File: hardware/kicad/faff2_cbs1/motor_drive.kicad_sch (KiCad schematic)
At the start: 89 parts, among them J1101 1x6 2.54mm, J1102 1x6 2.54mm, J1103 Micro-Fit 1x3, Q1101 BSZ099N06LS5, Q1102 BSZ099N06LS5, Q1103 BSZ099N06LS5, Q1104 BSZ099N06LS5, Q1105 BSZ099N06LS5, Q1106 BSZ099N06LS5, U1101 DRV8323S

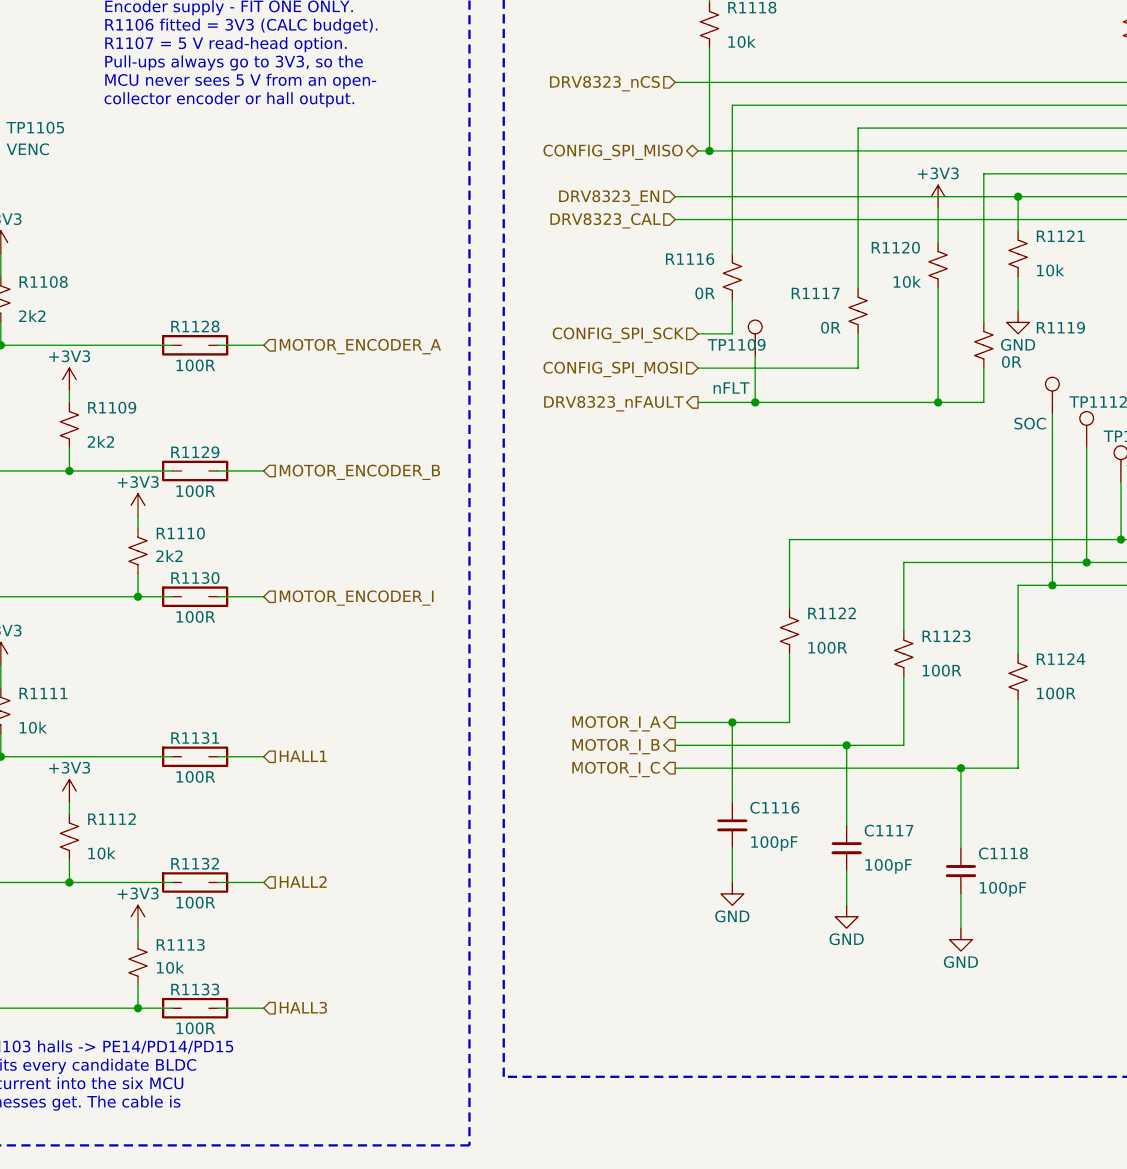
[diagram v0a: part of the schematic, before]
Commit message: review r4 items 7,8,13 and the PWR1131 ruling: parts, not placement
Items 7 and 8, R608 and R609 go. Review round R6 asked for DNP parallel
positions across R601, FB601 and D601; the captain has reversed two of the
three, and the reasoning is better than the original: R608 and R601 are the same
0603, so to meter head current you replace R601 with a shunt rather than
populate a second footprint beside it, and FB601 can be lifted and bridged
instead of fitting R609. D602 stays - a second clamp POSITION, for a different
clamp voltage or a bidirectional part, is not the same argument. Both the sheet
note and actuator-rev-afe.md's R6 row now carry the reversal rather than
quietly dropping it.

Item 13, R1128..R1133 were the only 100R in the design on a project-local
symbol: faff2_passives:RES_TF_100R_0603_H, a pre-rotated variant round 2 added
so they could lie horizontally without instance rotation - that was the reason,
and it does not outweigh nine other 100R across mcu, ui_io and motor_drive using
the house Amodo_Resistors:RES_TF_100R_0603. They unify onto it, rotated 90 with
field angles compensated to 270, which AGENTS.md permits on exactly that
condition and which a render confirms: horizontal body, horizontal text. The
local variant now has no users and is deleted from both the sheet and
faff2_passives, and AGENTS.md's guidance flips to prefer the house symbol.

The captain's third round-3 answer: R1120 and its +3V3 flag drag 7.62 mm down
into the clear space below, same connectivity, and the gate-drive bus no longer
crosses the arrow. No bus reroute, as instructed. Dropping it put R1120's
reference 0.02 mm off R1117's body, so the reference centres in the 6.85 mm
between the two.

The design is now clean under tools/check_text_clearance.py --margin 0.35 for
the first time - zero findings on all ten sheets.

ERC 0/0 at severity-all; 406 components, 264 nets. The only netlist change is
the two removals.

Co-Authored-By: Claude Opus 5 <noreply@anthropic.com>
Claude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
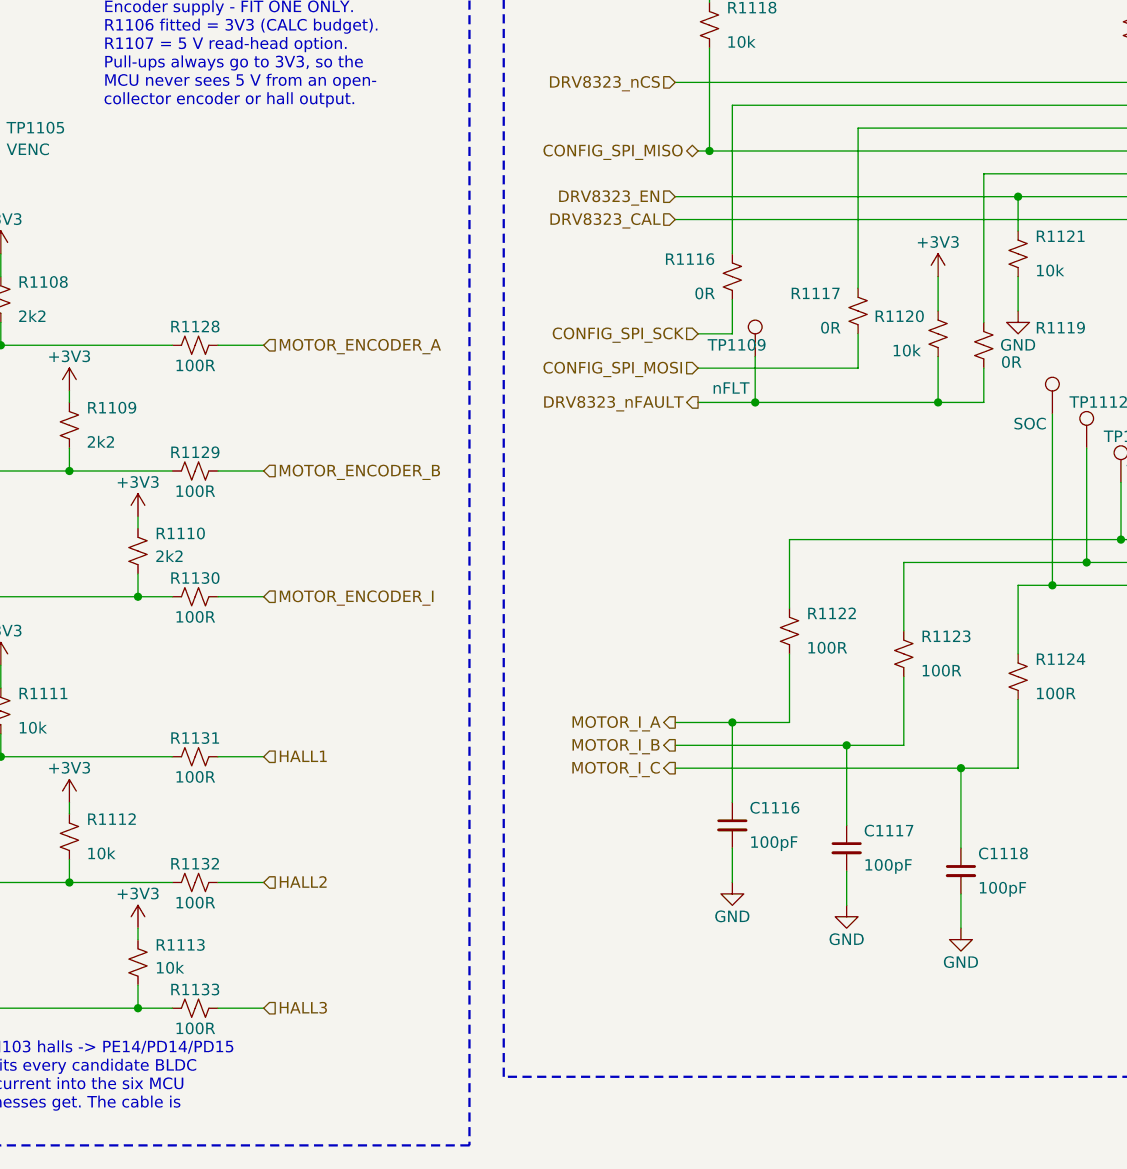
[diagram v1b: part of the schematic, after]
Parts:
- R1128, R1129, R1130, R1131, R1132, R1133: symbol faff2_passives:RES_TF_100R_0603_H -> Amodo_Resistors:RES_TF_100R_0603
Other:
- moved on the sheet: R1120

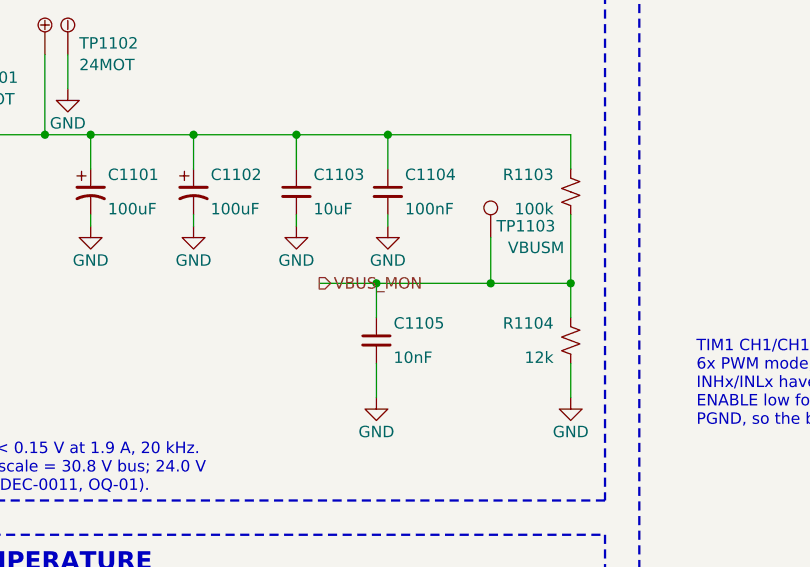
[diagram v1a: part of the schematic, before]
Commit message: review r4: the captain's two power answers - PG into RAIL_PGOOD, +5V5 to 6 V
A1. Both ADPL42005 power-good pins join DEC-P9's wired-AND. R317 and R318, 1 k
each like R315/R316, from each PG down to a local RAIL_PGOOD label - the idiom
the sheet already uses to reach that node three times. A dead 5 V rail is now
visible at D303 and TP308, which is the gap round 3 raised.

A2. +5V5 becomes 6.110 V nominal. The captain asked for 6.0 V - the
ADPL42005's characterised VIN = VOUT + 1 V point - or slightly above only if the
tolerance stack needs it to guarantee a 6.0 V minimum. It does: the LMR33630's
feedback reference is 0.985/1.000/1.015 V, +/-1.5% over the operating range, so
a 100k/20k divider gives 5.900/6.000/6.100 - nominal exactly on target, floor
100 mV short. 64.9k/12.7k gives 6.009/6.110/6.212 and the floor clears. Both
options and the arithmetic are in DEC-P10, along with what else moves: divider
impedance 122.1k to 77.6k so the 50 nA FB bias costs 3.2 mV, duty 0.255 at 24 V
in, caps still better than 2.5x derated, LDO dissipation 139 mW worst case.

Two traps on the way, both worth the tools that caught them. Hand-building the
new resistor block assembled its effects string with a str.replace on
"\t\t\t)", which also matched the font block's closing paren and put (hide yes)
inside it - KiCad answered "Failed to load schematic" and truncated the sheet to
349 components. The netlist component count is what caught it; ERC alone said
220 violations without saying why. New instances are cloned from an existing one
now. And set_lib_id alone left R303 and R304 carrying the OLD parts' mpn,
datasheet and description - a swap that looks right on the sheet and ships the
wrong part number to the BOM. sch_edit.sync_properties refreshes them from the
library, and both now read ERA-3AEB6492V and ERA-3AEB1272V.

ERC 0/0 at severity-all; 408 components, 264 nets; zero clearance findings. The
netlist change is exactly the two PG branches.

Co-Authored-By: Claude Opus 5 <norepl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
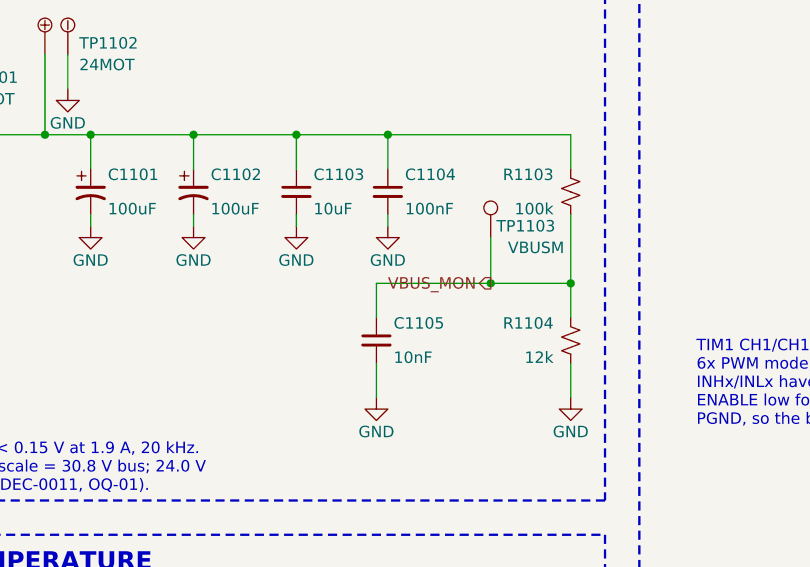
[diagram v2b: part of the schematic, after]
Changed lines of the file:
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@@
 	(hierarchical_label "VBUS_MON"
 		(shape output)
-		(at 82.55 77.47 180)
+		(at 101.6 77.47 180)
 		(effects
 			(font
 				(size 1.27 1.27)
 			)
-			(justify left bottom)
+			(justify right)
 		)
 	)
@@
 	(wire
 		(pts
-			(xy 82.55 77.47) (xy 88.9 77.47)
-		)
-		(stroke
-			(width 0)
-			(type default)
-		)
-	)
-	(wire
-		(pts
 			(xy 88.9 77.47) (xy 88.9 81.28)
 		)
@@
 		(diameter 0)
 		(color 0 0 0 0)
-	)
-	(junction
-		(at 88.9 77.47)
-		(diameter 0)
-		(color 0 0 0 0)
